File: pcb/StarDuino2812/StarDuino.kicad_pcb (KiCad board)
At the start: 2 copper layers, 126.3 x 120.3 mm, 68 parts, among them J1 Screw_Terminal_01x02, Q1 IRLML6401, U1 ATmega328P-AU, Y1 Crystal

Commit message: 2812 star in work
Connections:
- D10 pad 2: Net-(D10-Pad2) -> Net-(D1-Pad4)
- D11 pad 4: Net-(D10-Pad2) -> Net-(D11-Pad4)
- D12 pad 4: Net-(D11-Pad2) -> Net-(D12-Pad4)
- D14 pad 4: Net-(D13-Pad2) -> Net-(D14-Pad4)
- D15 pad 4: Net-(D14-Pad2) -> Net-(D15-Pad4)
- D16 pad 4: Net-(D15-Pad2) -> Net-(D16-Pad4)
- D18 pad 4: Net-(D17-Pad2) -> Net-(D18-Pad4)
- D19 pad 4: Net-(D18-Pad2) -> Net-(D19-Pad4)
- D2 pad 4: Net-(D1-Pad2) -> Net-(D11-Pad2)
- D20 pad 4: Net-(D19-Pad2) -> Net-(D20-Pad4)
- D22 pad 4: Net-(D21-Pad2) -> Net-(D22-Pad4)
- D23 pad 4: Net-(D22-Pad2) -> Net-(D23-Pad4)
- D24 pad 4: Net-(D23-Pad2) -> Net-(D24-Pad4)
- D26 pad 4: Net-(D25-Pad2) -> Net-(D26-Pad4)
- D27 pad 4: Net-(D26-Pad2) -> Net-(D27-Pad4)
- D28 pad 4: Net-(D27-Pad2) -> Net-(D28-Pad4)
- D3 pad 4: Net-(D2-Pad2) -> Net-(D12-Pad2)
- D30 pad 4: Net-(D29-Pad2) -> Net-(D30-Pad4)
- D31 pad 4: Net-(D30-Pad2) -> Net-(D31-Pad4)
- D32 pad 4: Net-(D31-Pad2) -> Net-(D32-Pad4)
- D34 pad 4: Net-(D33-Pad2) -> Net-(D34-Pad4)
- D35 pad 4: Net-(D34-Pad2) -> Net-(D35-Pad4)
- D36 pad 4: Net-(D35-Pad2) -> Net-(D36-Pad4)
- D38 pad 4: Net-(D37-Pad2) -> Net-(D38-Pad4)
- D39 pad 4: Net-(D38-Pad2) -> Net-(D39-Pad4)
- D4 pad 4: Net-(D3-Pad2) -> Net-(D4-Pad4)
- D40 pad 4: Net-(D39-Pad2) -> Net-(D40-Pad4)
- D42 pad 4: Net-(D41-Pad2) -> Net-(D42-Pad4)
- D43 pad 4: Net-(D42-Pad2) -> Net-(D43-Pad4)
- D44 pad 4: Net-(D43-Pad2) -> Net-(D44-Pad4)
- D46 pad 4: Net-(D45-Pad2) -> Net-(D46-Pad4)
- D47 pad 4: Net-(D46-Pad2) -> Net-(D47-Pad4)
- D48 pad 4: Net-(D47-Pad2) -> Net-(D48-Pad4)
- D5 pad 4: Net-(D5-Pad4) -> Net-(D1-Pad2)
- D50 pad 4: Net-(D49-Pad2) -> Net-(D50-Pad4)
- D51 pad 4: Net-(D50-Pad2) -> Net-(D51-Pad4)
- D52 pad 4: Net-(D51-Pad2) -> Net-(D52-Pad4)
- D54 pad 4: Net-(D53-Pad2) -> Net-(D54-Pad4)
- D55 pad 4: Net-(D54-Pad2) -> Net-(D55-Pad4)
- D56 pad 4: Net-(D55-Pad2) -> Net-(D56-Pad4)
- D58 pad 4: Net-(D57-Pad2) -> Net-(D58-Pad4)
- D59 pad 4: Net-(D58-Pad2) -> Net-(D59-Pad4)
- D6 pad 2: Net-(D6-Pad2) -> Net-(D10-Pad4)
- D6 pad 4: Net-(D5-Pad2) -> Net-(D2-Pad2)
- D60 pad 4: Net-(D59-Pad2) -> Net-(D60-Pad4)
- D7 pad 2: Net-(D7-Pad2) -> Net-(D11-Pad4)
- D7 pad 4: Net-(D6-Pad2) -> Net-(D3-Pad2)
- D8 pad 2: Net-(D8-Pad2) -> Net-(D12-Pad4)
- D8 pad 4: Net-(D7-Pad2) -> Net-(D4-Pad2)
- D9 pad 2: Net-(D10-Pad4) -> Net-(D9-Pad2)
- D9 pad 4: Net-(D9-Pad4) -> Net-(D5-Pad2)
- U1 pad 7: Net-(U1-Pad7) -> Net-(C2-Pad1)
- U1 pad 8: Net-(U1-Pad8) -> Net-(C1-Pad1)
- Y1 pad 1: Net-(Y1-Pad1) -> Net-(C1-Pad1)
- Y1 pad 2: Net-(Y1-Pad2) -> Net-(C2-Pad1)
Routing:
- net VCC: track 0.00 -> 105.4 mm
- net GND: track 0.00 -> 94.2 mm
- net Net-(D12-Pad2): track 0.00 -> 22.9 mm
- net Net-(D11-Pad2): track 0.00 -> 21.1 mm
- net Net-(D5-Pad2): track 0.00 -> 17.0 mm
- net Net-(D1-Pad4): track 0.00 -> 16.9 mm
- net Net-(D10-Pad4): track 0.00 -> 11.9 mm
- net Net-(D4-Pad2): track 0.00 -> 11.6 mm
- net Net-(D11-Pad4): track 0.00 -> 9.38 mm
- net Net-(D3-Pad2): track 0.00 -> 8.13 mm
- net Net-(D2-Pad2): track 0.00 -> 5.07 mm
- net Net-(D12-Pad4): track 0.00 -> 4.80 mm
- net Net-(D1-Pad2): track 0.00 -> 2.73 mm

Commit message: 2812 star in work
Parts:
- moved C1 78.9 mm to (138.1, 107.0)
- moved C2 73.6 mm to (141.8, 95.9)
- moved Y1 72.6 mm to (135.5, 100.4), turned to 72 degrees
- moved U1 17.9 mm to (125.1, 95.2), turned to 180 degrees
- moved D33 10.7 mm to (74.1, 54.1)
- moved D10 10.7 mm to (111.0, 127.4)
- moved D56 10.7 mm to (119.1, 95.4)
- moved H1 10.7 mm to (104.7, 90.7)
- moved D19 10.7 mm to (77.7, 99.6)
- moved D3 10.7 mm to (95.8, 118.5)
- moved D6 10.7 mm to (104.7, 129.3)
- moved D60 10.7 mm to (125.1, 89.5)
- moved D20 10.7 mm to (90.4, 95.4)
- moved D42 10.7 mm to (127.6, 59.5)
- moved D23 10.7 mm to (81.1, 107.9)
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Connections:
- D17 pad 4: Net-(D17-Pad4) -> Net-(D13-Pad2)
- D18 pad 4: Net-(D18-Pad4) -> Net-(D14-Pad2)
- D19 pad 4: Net-(D19-Pad4) -> Net-(D15-Pad2)
- D20 pad 4: Net-(D20-Pad4) -> Net-(D16-Pad2)
- D21 pad 4: Net-(D21-Pad4) -> Net-(D17-Pad2)
- D22 pad 2: Net-(D22-Pad2) -> Net-(D13-Pad4)
- D22 pad 4: Net-(D22-Pad4) -> Net-(D18-Pad2)
- D23 pad 2: Net-(D23-Pad2) -> Net-(D14-Pad4)
- D23 pad 4: Net-(D23-Pad4) -> Net-(D19-Pad2)
- D24 pad 2: Net-(D24-Pad2) -> Net-(D15-Pad4)
- D24 pad 4: Net-(D24-Pad4) -> Net-(D20-Pad2)
- D28 pad 4: Net-(D28-Pad4) -> Net-(D21-Pad2)
- D29 pad 4: Net-(D29-Pad4) -> Net-(D25-Pad2)
- D30 pad 4: Net-(D30-Pad4) -> Net-(D26-Pad2)
- D31 pad 4: Net-(D31-Pad4) -> Net-(D27-Pad2)
- D32 pad 4: Net-(D32-Pad4) -> Net-(D28-Pad2)
- D33 pad 4: Net-(D33-Pad4) -> Net-(D29-Pad2)
- D34 pad 2: Net-(D34-Pad2) -> Net-(D25-Pad4)
- D34 pad 4: Net-(D34-Pad4) -> Net-(D30-Pad2)
- D35 pad 2: Net-(D35-Pad2) -> Net-(D26-Pad4)
- D35 pad 4: Net-(D35-Pad4) -> Net-(D31-Pad2)
- D36 pad 2: Net-(D36-Pad2) -> Net-(D27-Pad4)
- D36 pad 4: Net-(D36-Pad4) -> Net-(D32-Pad2)
- D40 pad 4: Net-(D40-Pad4) -> Net-(D33-Pad2)
- D41 pad 4: Net-(D41-Pad4) -> Net-(D37-Pad2)
- D42 pad 4: Net-(D42-Pad4) -> Net-(D38-Pad2)
- D43 pad 4: Net-(D43-Pad4) -> Net-(D39-Pad2)
- D44 pad 4: Net-(D44-Pad4) -> Net-(D40-Pad2)
- D45 pad 4: Net-(D45-Pad4) -> Net-(D41-Pad2)
- D46 pad 2: Net-(D46-Pad2) -> Net-(D37-Pad4)
- D46 pad 4: Net-(D46-Pad4) -> Net-(D42-Pad2)
- D47 pad 2: Net-(D47-Pad2) -> Net-(D38-Pad4)
- D47 pad 4: Net-(D47-Pad4) -> Net-(D43-Pad2)
- D48 pad 2: Net-(D48-Pad2) -> Net-(D39-Pad4)
- D48 pad 4: Net-(D48-Pad4) -> Net-(D44-Pad2)
- D52 pad 4: Net-(D52-Pad4) -> Net-(D45-Pad2)
- D53 pad 4: Net-(D53-Pad4) -> Net-(D49-Pad2)
- D54 pad 4: Net-(D54-Pad4) -> Net-(D50-Pad2)
- D55 pad 4: Net-(D55-Pad4) -> Net-(D51-Pad2)
- D56 pad 4: Net-(D56-Pad4) -> Net-(D52-Pad2)
- D57 pad 4: Net-(D57-Pad4) -> Net-(D53-Pad2)
- D58 pad 2: Net-(D58-Pad2) -> Net-(D49-Pad4)
- D58 pad 4: Net-(D58-Pad4) -> Net-(D54-Pad2)
- D59 pad 2: Net-(D59-Pad2) -> Net-(D50-Pad4)
- D59 pad 4: Net-(D59-Pad4) -> Net-(D55-Pad2)
- D60 pad 2: Net-(D60-Pad2) -> Net-(D51-Pad4)
- D60 pad 4: Net-(D60-Pad4) -> Net-(D56-Pad2)
- D9 pad 2: Net-(D9-Pad2) -> Net-(D16-Pad4)
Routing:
- net GND: track 94.2 -> 579.9 mm
- net VCC: track 105.4 -> 526.8 mm
- net Net-(D39-Pad4): track 0.00 -> 22.9 mm
- net Net-(D27-Pad4): track 0.00 -> 22.9 mm
- net Net-(D51-Pad4): track 0.00 -> 22.9 mm
- net Net-(D15-Pad4): track 0.00 -> 22.9 mm
- net Net-(D38-Pad4): track 0.00 -> 21.1 mm
- net Net-(D50-Pad4): track 0.00 -> 21.1 mm
- net Net-(D26-Pad4): track 0.00 -> 21.1 mm
- net Net-(D14-Pad4): track 0.00 -> 21.1 mm
- net Net-(D17-Pad2): track 0.00 -> 17.1 mm
- net Net-(D53-Pad2): track 0.00 -> 17.0 mm
- net Net-(D41-Pad2): track 0.00 -> 17.0 mm
- net Net-(D29-Pad2): track 0.00 -> 17.0 mm
- net Net-(D49-Pad4): track 0.00 -> 16.9 mm
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
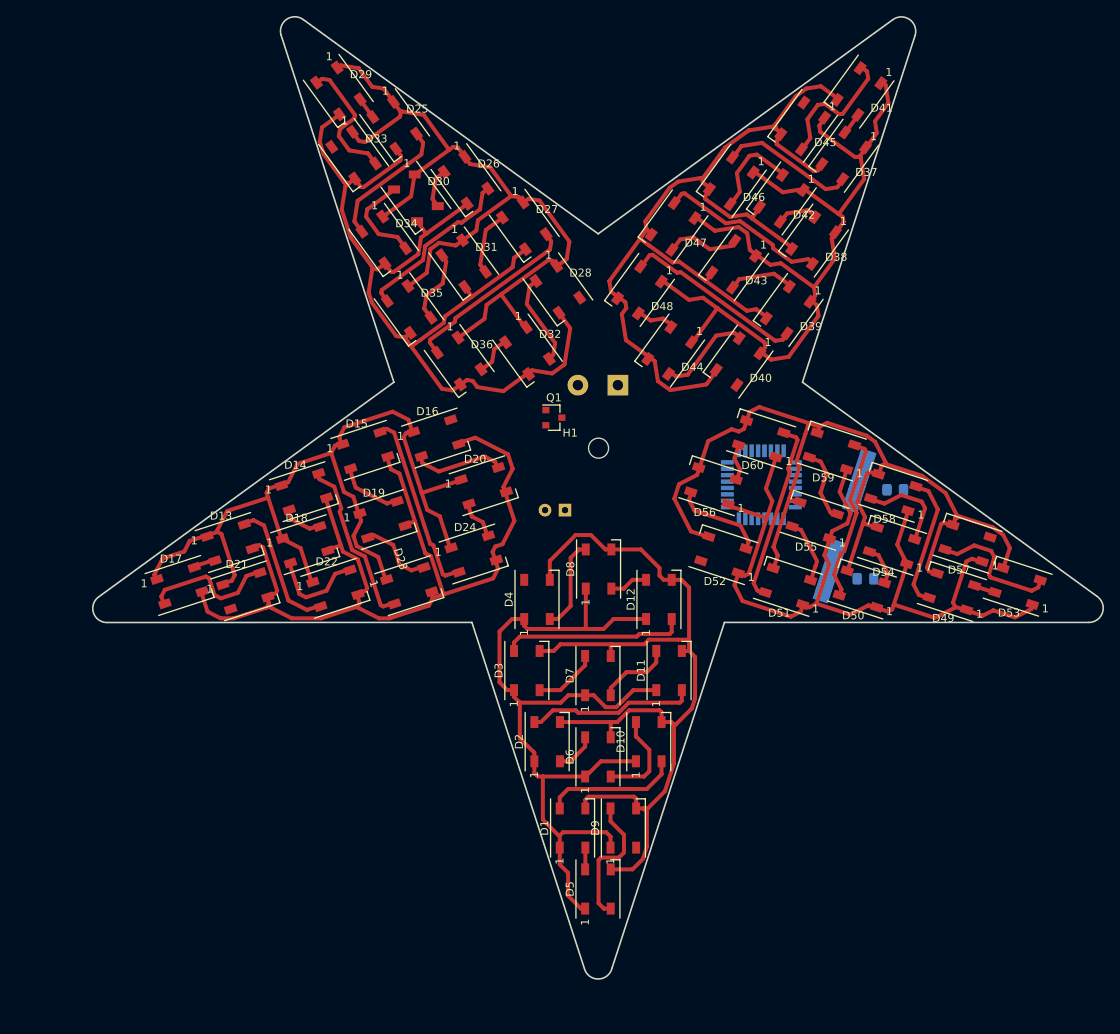
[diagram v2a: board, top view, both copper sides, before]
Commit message: Cut vertexes
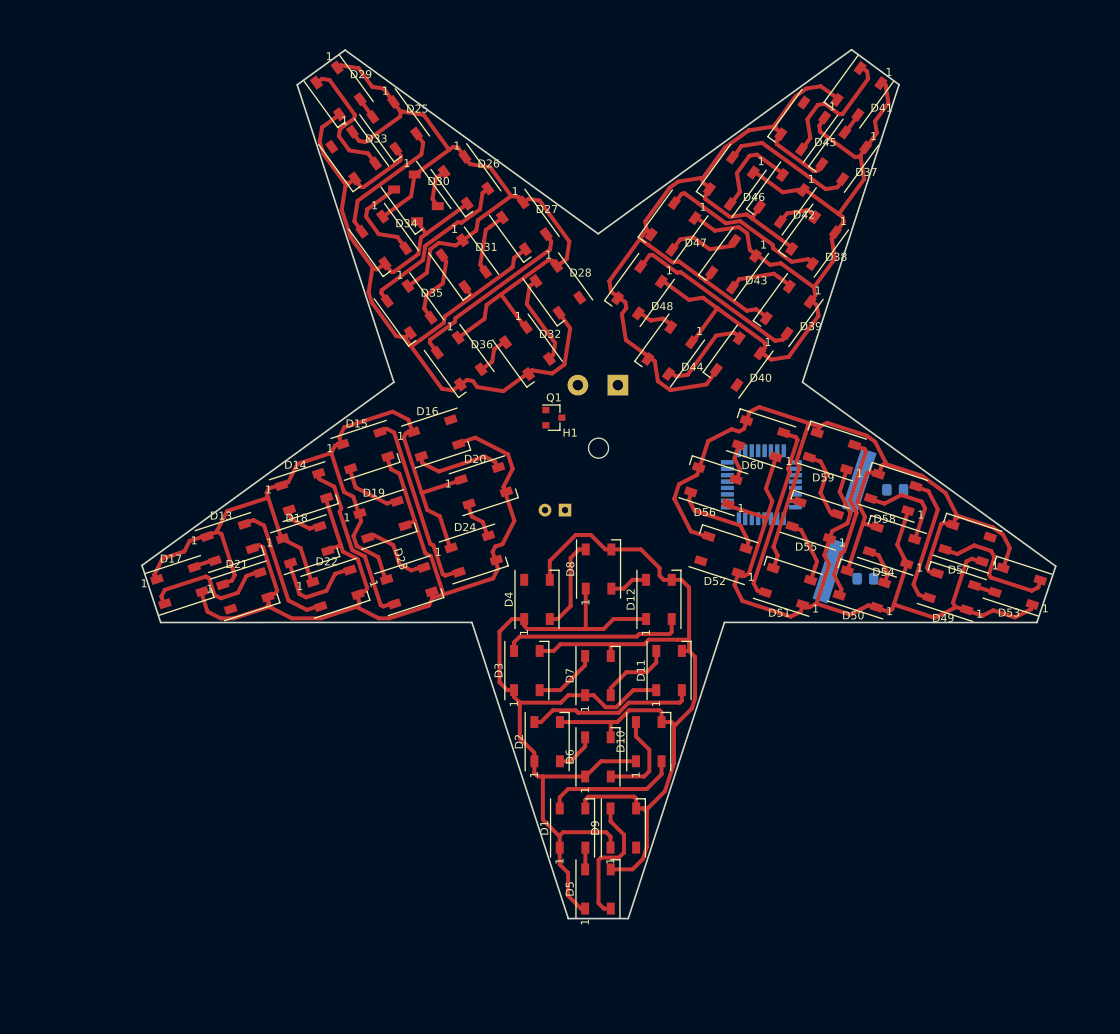
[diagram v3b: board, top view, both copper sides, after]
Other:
- board size 126.3 x 120.3 mm -> 114.2 x 108.6 mm

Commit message: Almost ready
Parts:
- added C4: 0.1uF, Capacitor_SMD:C_0805_2012Metric_Pad1.18x1.45mm_HandSolder, F.Cu at (100.1, 99.1)
- added H2: MountingHole, MountingHole:MountingHole_2.5mm, F.Cu at (119.6, 111.0)
- added H3: MountingHole, MountingHole:MountingHole_2.5mm, F.Cu at (128.5, 82.9)
- added H4: MountingHole, MountingHole:MountingHole_2.5mm, F.Cu at (89.9, 111.1)
- added J2: Conn_01x03_Male, Connector_PinHeader_2.54mm:PinHeader_1x03_P2.54mm_Vertical, B.Cu at (110.8, 103.5)
- added R1: 1M, Resistor_SMD:R_0805_2012Metric_Pad1.20x1.40mm_HandSolder, F.Cu at (114.4, 88.4)
- added R2: 10k, Resistor_SMD:R_0805_2012Metric_Pad1.20x1.40mm_HandSolder, F.Cu at (99.4, 101.1)
- C1, C2, U1: moved to F.Cu
- Y1: value Crystal -> 16M; footprint Crystal:Crystal_SMD_HC49-SD_HandSoldering -> Crystal:Crystal_HC49-4H_Vertical
- moved C1 30.9 mm to (116.7, 84.7), turned to 45 degrees
- moved Y1 26.4 mm to (113.5, 85.7), turned to 315 degrees
- moved C2 25.5 mm to (118.2, 86.2), turned to 45 degrees
- moved H1 25.0 mm to (104.7, 65.7)
- moved U1 17.5 mm to (107.6, 94.6), turned to 230 degrees
- moved C3 9.33 mm to (96.2, 90.2), turned to 315 degrees
- moved J1 4.96 mm to (102.2, 82.2), turned to 0 degrees
- moved Q1 1.10 mm to (98.4, 86.0)
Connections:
- U1 pad 18: Net-(U1-Pad18) -> VCC
- U1 pad 24: Net-(U1-Pad24) -> Net-(D4-Pad4)
- U1 pad 29: Net-(U1-Pad29) -> /~Reset
- U1 pad 30: Net-(U1-Pad30) -> /RX
- U1 pad 31: Net-(U1-Pad31) -> /TX
- U1 pad 4: Net-(U1-Pad4) -> VCC
- U1 pad 6: Net-(U1-Pad4) -> VCC
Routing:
- net VCC: track 526.8 -> 709.7 mm, vias 0 -> 6
- net GND: track 579.9 -> 718.4 mm, vias 0 -> 2
- net Net-(D16-Pad4): track 0.00 -> 78.9 mm, vias 0 -> 2
- net Net-(D33-Pad2): track 0.00 -> 78.3 mm, vias 0 -> 2
- net Net-(D21-Pad2): track 0.00 -> 73.2 mm, vias 0 -> 2
- net Net-(D45-Pad2): track 0.00 -> 68.7 mm, vias 0 -> 2
- net /~Reset: track 0.00 -> 18.4 mm
- net Net-(D4-Pad4): track 0.00 -> 18.3 mm, vias 0 -> 2
- net Net-(C2-Pad1): track 0.00 -> 13.0 mm
- net Net-(C1-Pad1): track 0.00 -> 11.7 mm
- net /RX: track 0.00 -> 5.71 mm
- net Net-(J1-Pad1): track 0.00 -> 5.69 mm
- net /TX: track 0.00 -> 5.02 mm
- net Net-(D40-Pad2): track 11.6 -> 13.8 mm
- net Net-(D52-Pad2): track 11.6 -> 11.0 mm

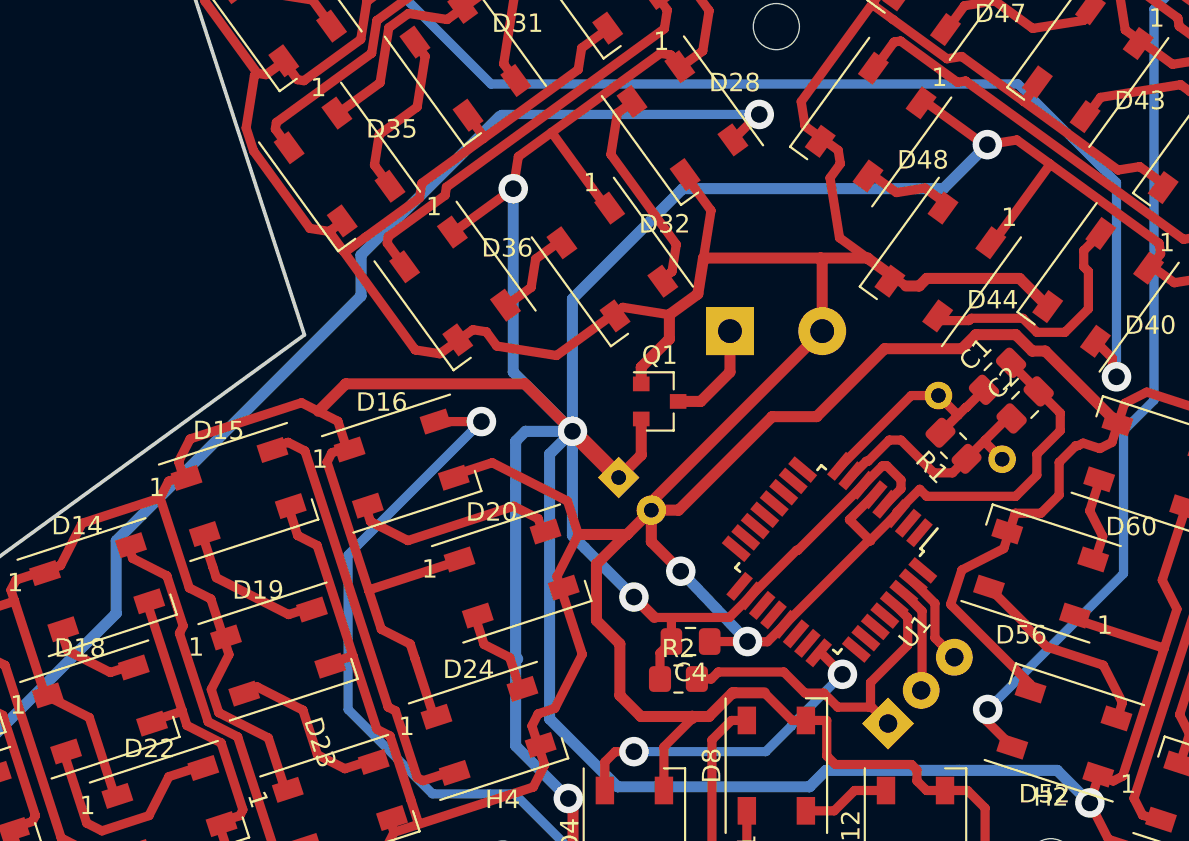
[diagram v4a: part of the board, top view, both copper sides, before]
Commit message: Add fifth hole
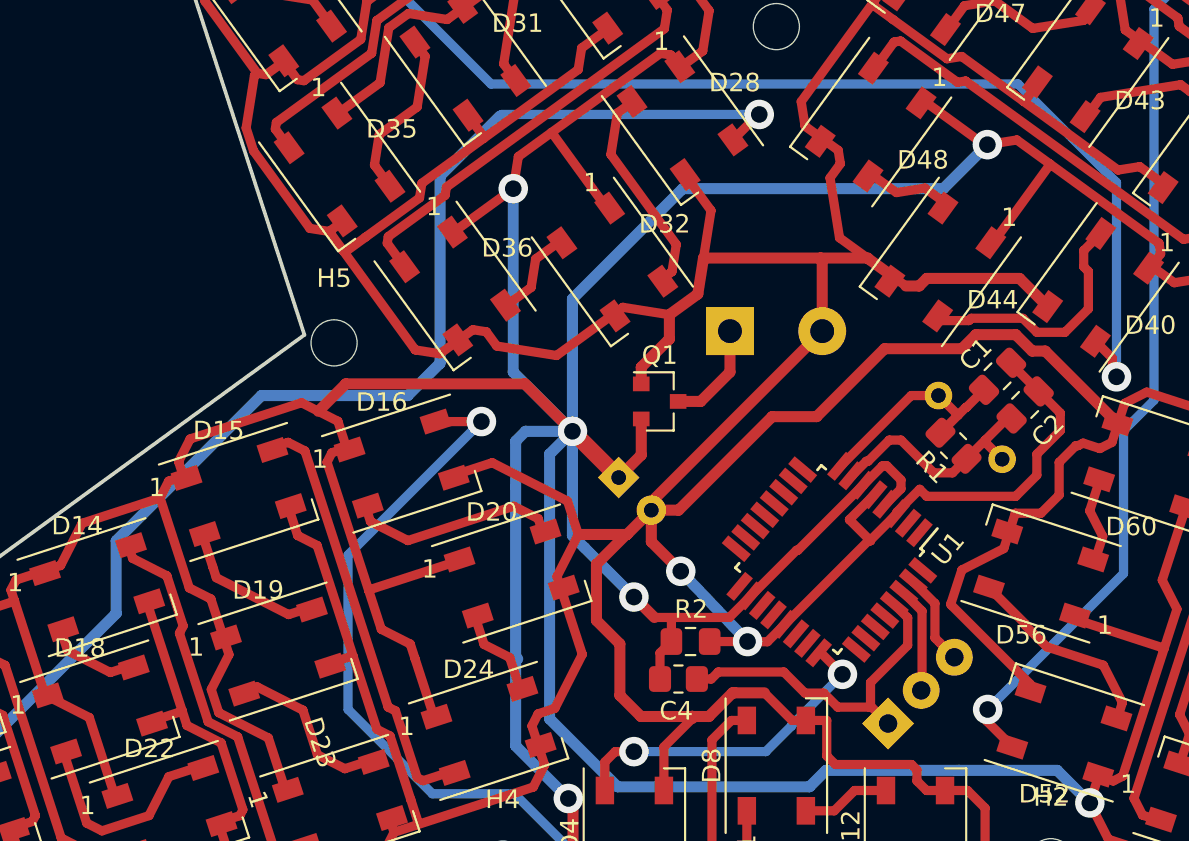
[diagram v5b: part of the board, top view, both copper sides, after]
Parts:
- added H5: MountingHole, MountingHole:MountingHole_2.5mm, F.Cu at (80.8, 82.9)
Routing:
- net Net-(D21-Pad2): track 73.2 -> 77.9 mm
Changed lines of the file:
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@@
     (thickness 1.6)
     (drawings 22)
-    (tracks 1065)
+    (tracks 1067)
     (zones 0)
-    (modules 75)
+    (modules 76)
     (nets 90)
   )
@@
   )
   (setup
-    (last_trace_width 0.6)
+    (last_trace_width 0.25)
     (user_trace_width 0.5)
     (user_trace_width 0.6)
@@
       (effects (font (size 1 1) (thickness 0.15)) (justify mirror))
     )
-    (fp_text user %R (at 0 -2.54 225) (layer B.Fab)
-      (effects (font (size 1 1) (thickness 0.15)) (justify mirror))
-    )
     (fp_line (start -0.635 1.27) (end 1.27 1.27) (layer B.Fab) (width 0.1))
     (fp_line (start 1.27 1.27) (end 1.27 -6.35) (layer B.Fab) (width 0.1))
@@
     (fp_line (start 1.8 -6.85) (end 1.8 1.8) (layer B.CrtYd) (width 0.05))
     (fp_line (start 1.8 1.8) (end -1.8 1.8) (layer B.CrtYd) (width 0.05))
+    (fp_text user %R (at 0 -2.54 225) (layer B.Fab)
+      (effects (font (size 1 1) (thickness 0.15)) (justify mirror))
+    )
     (pad 3 thru_hole oval (at 0 -5.079999 315) (size 2 2) (drill 1) (layers *.Cu *.Mask)
       (net 89 /TX))
@@
     (tags "capacitor handsolder")
     (attr smd)
-    (fp_text reference C4 (at 0 -1.68) (layer F.SilkS)
+    (fp_text reference C4 (at 0.7775 -3.76) (layer F.SilkS)
       (effects (font (size 1 1) (thickness 0.15)))
     )
@@
     (tags "capacitor handsolder")
     (attr smd)
-    (fp_text reference C2 (at 0 -1.68 45) (layer F.SilkS)
+    (fp_text reference C2 (at -0.108894 1.85262 45) (layer F.SilkS)
       (effects (font (size 1 1) (thickness 0.15)))
     )
@@
     (tags "QFP 0.8")
     (attr smd)
-    (fp_text reference U1 (at 0 -6.05 50) (layer F.SilkS)
+    (fp_text reference U1 (at -4.587314 -4.541292 50) (layer F.SilkS)
       (effects (font (size 1 1) (thickness 0.15)))
     )
@@
     (tags "resistor handsolder")
     (attr smd)
-    (fp_text reference R2 (at 0 -1.65) (layer F.SilkS)
+    (fp_text reference R2 (at 0.689 -3.782) (layer F.SilkS)
       (effects (font (size 1 1) (thickness 0.15)))
     )
@@
     )
   )
+  (module MountingHole:MountingHole_2.5mm (layer F.Cu)
+    (at 80.772 82.8675)
+    (descr "Mounting Hole 2.5mm, no annular")
+    (tags "mounting hole 2.5mm no annular")
+    (attr virtual)
+    (fp_text reference H5 (at 0 -3.5) (layer F.SilkS)
+      (effects (font (size 1 1) (thickness 0.15)))
+    )
+    (fp_text value MountingHole (at 0 3.5) (layer F.Fab)
+      (effects (font (size 1 1) (thickness 0.15)))
+    )
+    (fp_circle (center 0 0) (end 2.75 0) (layer F.CrtYd) (width 0.05))
+    (fp_circle (center 0 0) (end 2.5 0) (layer Cmts.User) (width 0.15))
+    (fp_text user %R (at 0.3 0) (layer F.Fab)
+      (effects (font (size 1 1) (thickness 0.15)))
+    )
+    (pad 1 np_thru_hole circle (at 0 0) (size 2.5 2.5) (drill 2.5) (layers *.Cu *.Mask))
+  )
   (gr_line (start 136.3726 40.8686) (end 142.3162 45.2374) (layer Edge.Cuts) (width 0.2))
   (gr_line (start 67.0814 45.2628) (end 73.0758 40.9194) (layer Edge.Cuts) (width 0.2))
@@
   (segment (start 56.134 110.363) (end 68.961 97.536) (width 0.6) (layer B.Cu) (net 21))
   (segment (start 68.961 97.536) (end 68.961 93.599) (width 0.6) (layer B.Cu) (net 21))
-  (segment (start 68.961 93.599) (end 82.2325 80.3275) (width 0.6) (layer B.Cu) (net 21))
-  (segment (start 82.2325 80.3275) (end 82.2325 78.105) (width 0.6) (layer B.Cu) (net 21))
   (segment (start 89.8525 70.485) (end 89.75725 70.58025) (width 0.5) (layer B.Cu) (net 21))
   (segment (start 103.8225 70.485) (end 89.8525 70.485) (width 0.5) (layer B.Cu) (net 21))
-  (segment (start 82.2325 78.105) (end 89.75725 70.58025) (width 0.6) (layer B.Cu) (net 21))
+  (segment (start 76.835 85.725) (end 84.7725 85.725) (width 0.6) (layer B.Cu) (net 21))
+  (segment (start 68.961 93.599) (end 76.835 85.725) (width 0.6) (layer B.Cu) (net 21))
+  (segment (start 86.51875 83.97875) (end 86.51875 73.81875) (width 0.6) (layer B.Cu) (net 21))
+  (segment (start 84.7725 85.725) (end 86.51875 83.97875) (width 0.6) (layer B.Cu) (net 21))
+  (segment (start 86.51875 73.81875) (end 89.75725 70.58025) (width 0.6) (layer B.Cu) (net 21))
   (segment (start 74.962543 47.135734) (end 74.968075 47.100814) (width 0.5) (layer F.Cu) (net 22))
   (segment (start 76.546625 49.316035) (end 74.962543 47.135734) (width 0.5) (layer F.Cu) (net 22))

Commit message: Fix tracks
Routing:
- net Net-(D16-Pad4): track 78.9 -> 70.3 mm
- net Net-(D21-Pad2): track 77.9 -> 75.7 mm
- net VCC: track 709.7 -> 708.8 mm
